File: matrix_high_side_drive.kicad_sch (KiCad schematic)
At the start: 46 parts, among them Q10 DMC2400UV-7, Q11 DMC2400UV-7, Q12 DMC2400UV-7, Q13 DMC2400UV-7, Q14 DMC2400UV-7, Q15 DMC2400UV-7, Q16 DMC2400UV-7, Q17 DMC2400UV-7, Q18 DMC2400UV-7, Q19 DMC2400UV-7, Q20 DMC2400UV-7, Q7 DMC2400UV-7, Q8 DMC2400UV-7, Q9 DMC2400UV-7

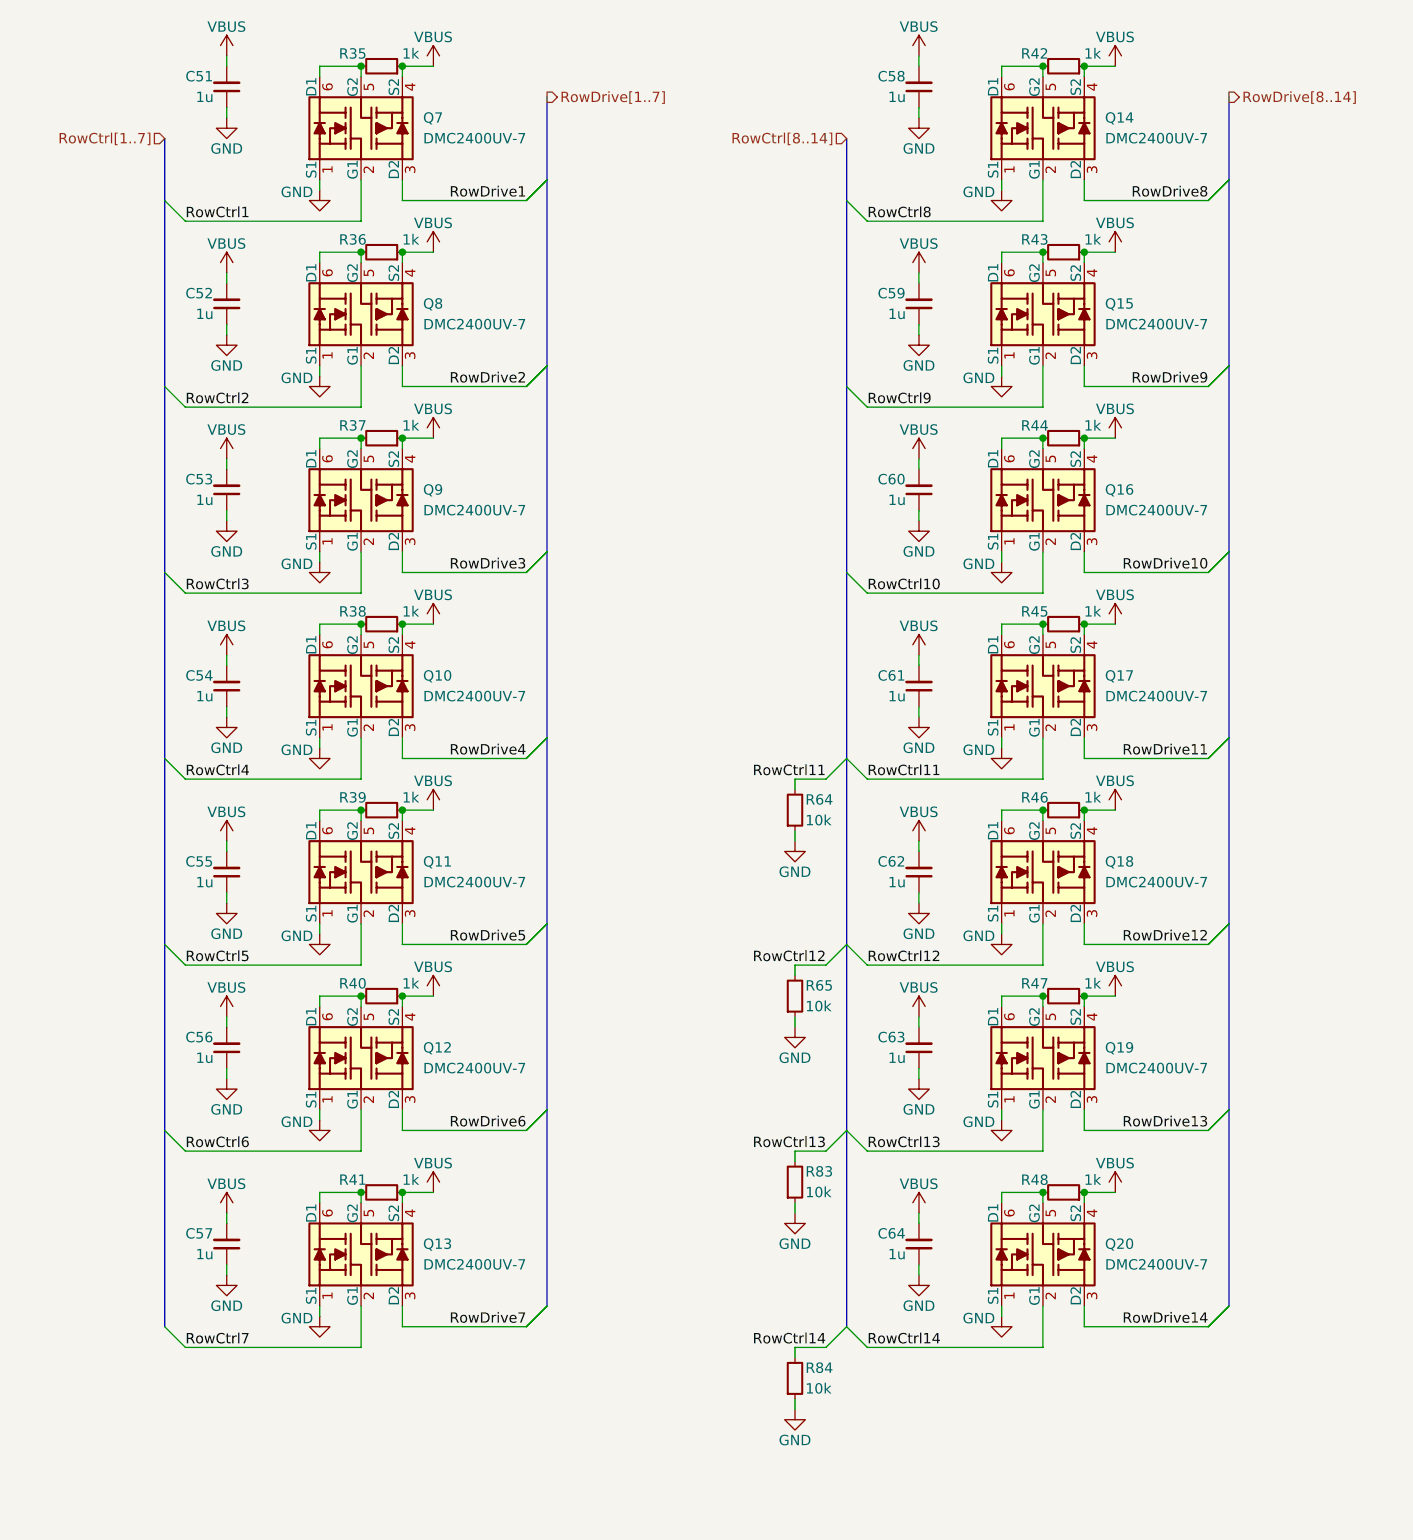
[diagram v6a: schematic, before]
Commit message: [#72133] Add captions to schematic sheets
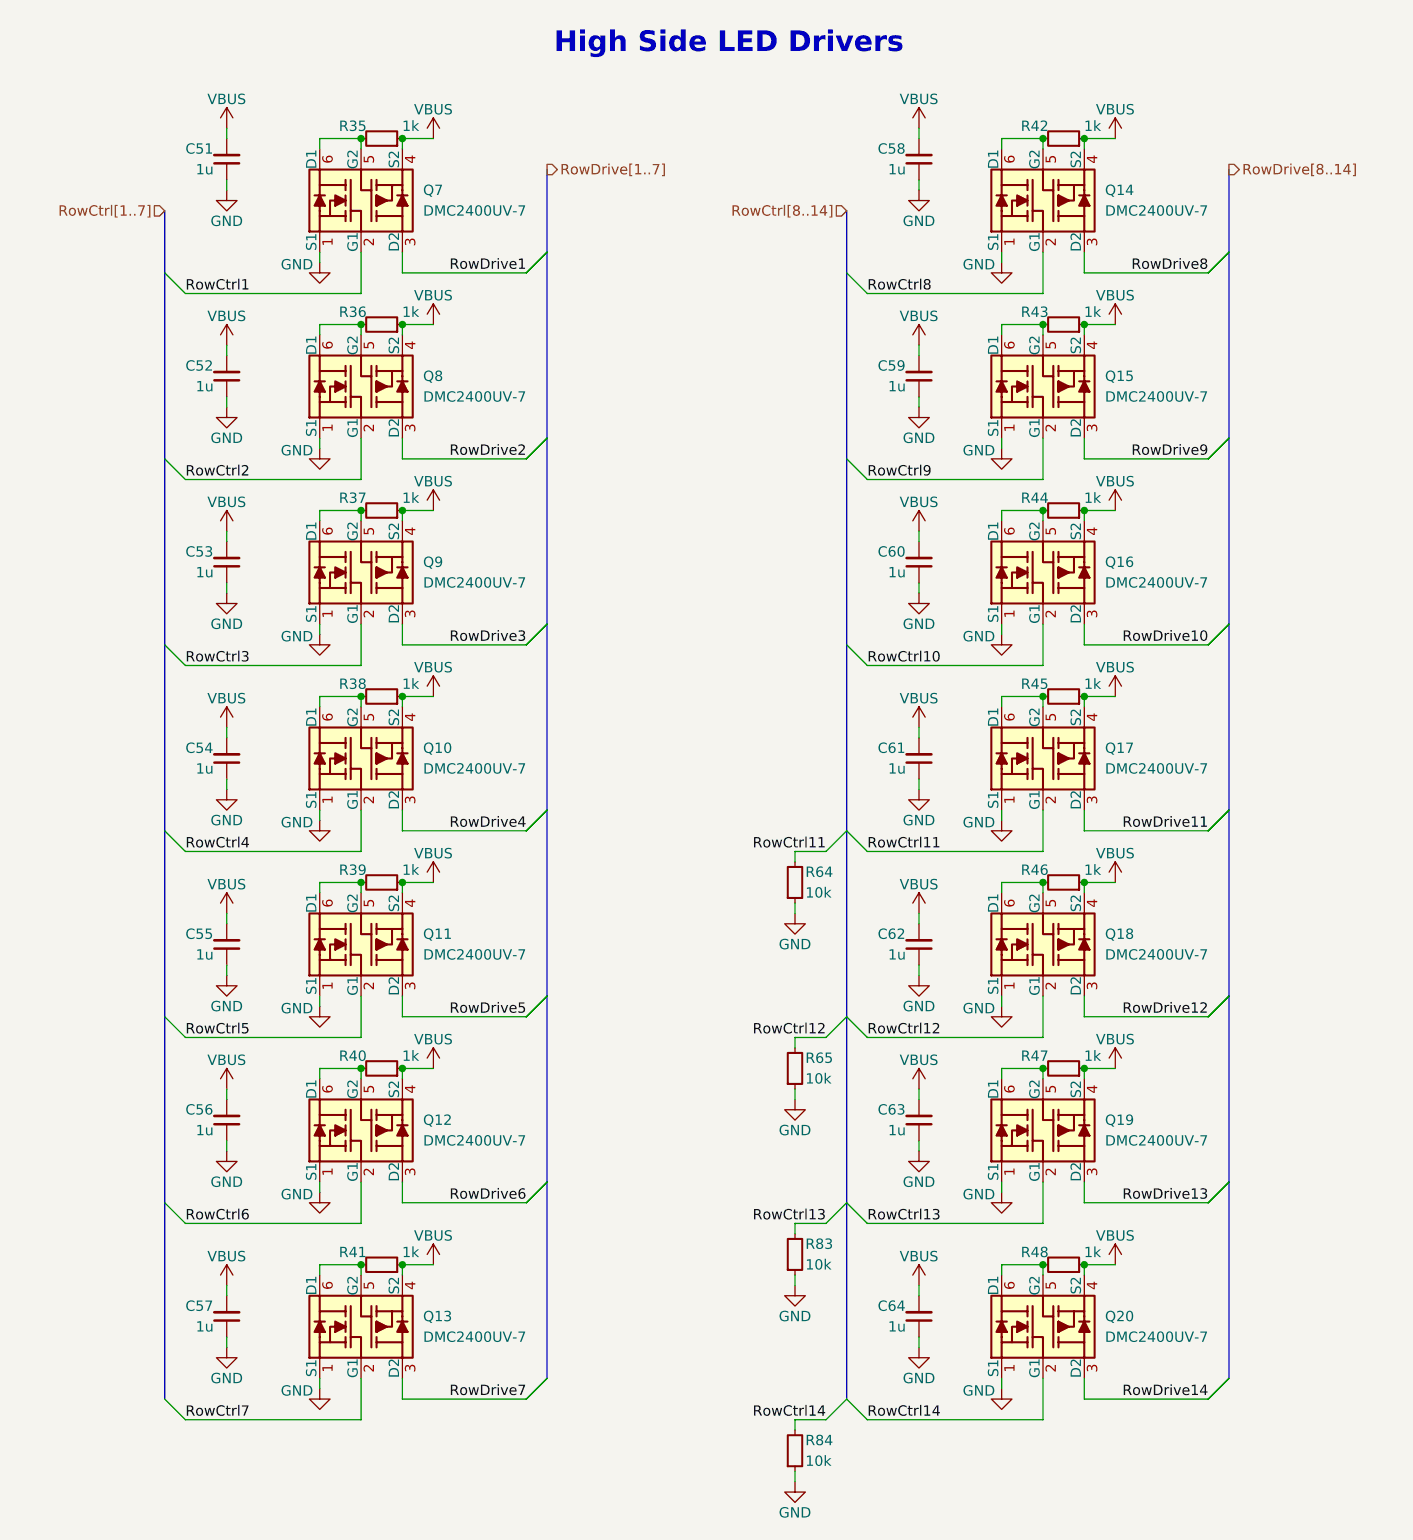
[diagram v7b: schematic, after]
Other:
- note added: "High Side LED Drivers"
- moved on the sheet: C51, C52, C53, C54, C55, C56, C57, C58, C59, C60, C61, C62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

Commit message: [#72447] SCH: Update matrix drive resistors
Signed-off-by: Dawid Lentka <dlentka@antmicro.com>
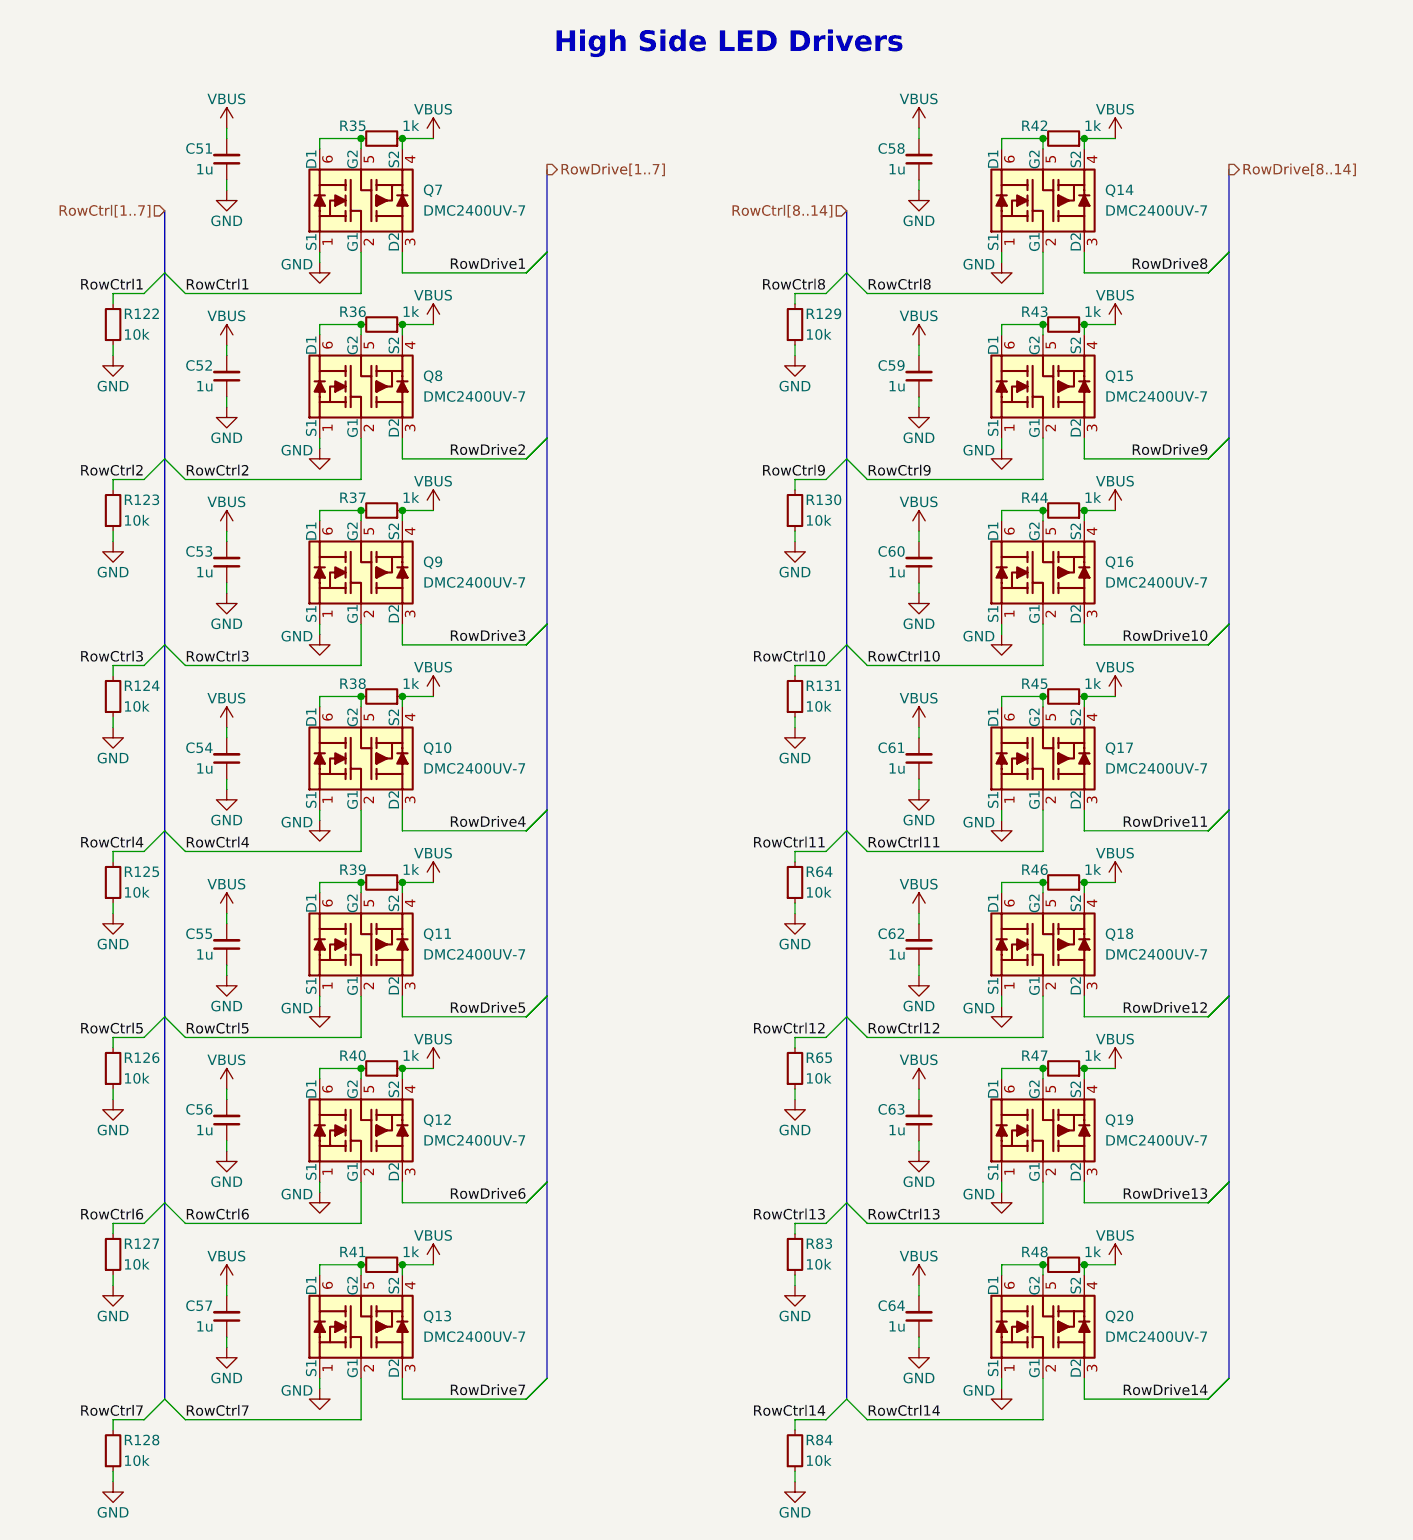
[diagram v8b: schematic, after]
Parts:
- added R122, R123, R124, R125, R126, R127, R128, R129, R130, R131: R_10k_0402, antmicro-footprints:R_0402_1005Metric, symbol antmicroResistors0402:R_10k_0402
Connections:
- net GND: now also R122.1, R123.1, R124.1, R125.1, R126.1, R127.1, R128.1, R129.1, R130.1, R131.1
- net RowCtrl1: now also R122.2
- net RowCtrl10: now also R131.2
- net RowCtrl2: now also R123.2
- net RowCtrl3: now also R124.2
- net RowCtrl4: now also R125.2
- net RowCtrl5: now also R126.2
- net RowCtrl6: now also R127.2
- net RowCtrl7: now also R128.2
- net RowCtrl8: now also R129.2
- net RowCtrl9: now also R130.2
